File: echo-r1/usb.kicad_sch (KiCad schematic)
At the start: 14 parts, among them J2 TYPE-C-31-M-12, Q5 AO3401A, U8 USB3320C-EZK

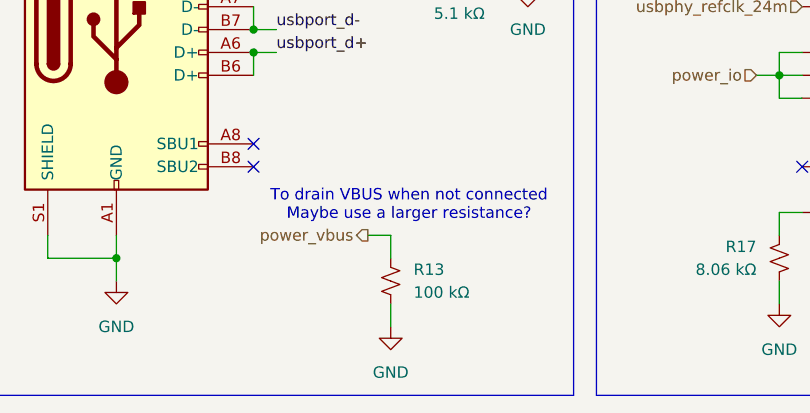
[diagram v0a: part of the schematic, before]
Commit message: R1-Rev1: remove VBUS discharge resistor
This is not needed since there is a path through the ADC
voltage divider to discharge VBUS -- and realistically
the battery charger should also discharge VBUS even with
no resistive path to ground.
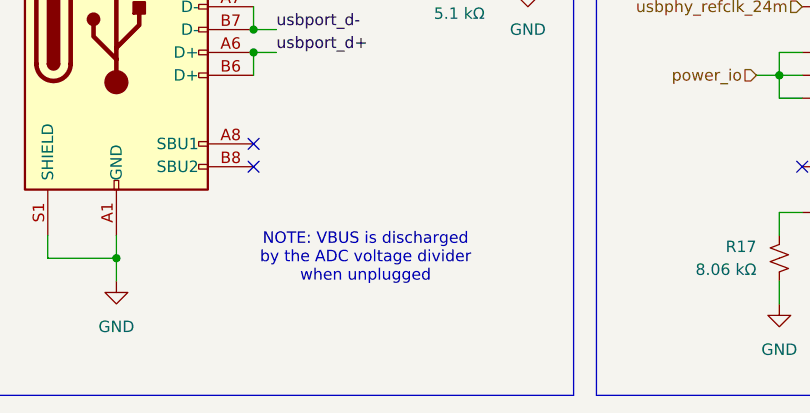
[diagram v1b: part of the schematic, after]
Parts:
- removed R13: 100 kΩ, Resistor_SMD:R_0402_1005Metric, symbol Device:R_Small_US
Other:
- note added: "NOTE: VBUS is discharged by the ADC voltage divider when unplugged"
- note removed: "To drain VBUS when not connected Maybe use a larger resistance?"
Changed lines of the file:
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@@
 		)
 	)
-	(text "To drain VBUS when not connected\nMaybe use a larger resistance?"
+	(text "NOTE: VBUS is discharged\nby the ADC voltage divider\nwhen unplugged"
 		(exclude_from_sim no)
-		(at 101.092 131.318 0)
+		(at 96.266 137.16 0)
 		(effects
 			(font
@@
 	(wire
 		(pts
-			(xy 99.06 142.24) (xy 99.06 144.78)
-		)
-		(stroke
-			(width 0)
-			(type default)
-		)
-	)
-	(wire
-		(pts
 			(xy 114.3 101.6) (xy 114.3 104.14)
 		)
@@
 	(wire
 		(pts
-			(xy 99.06 137.16) (xy 99.06 134.62)
-		)
-		(stroke
-			(width 0)
-			(type default)
-		)
-	)
-	(wire
-		(pts
 			(xy 236.22 66.04) (xy 236.22 63.5)
 		)
@@
 		)
 	)
-	(wire
-		(pts
-			(xy 99.06 134.62) (xy 96.52 134.62)
-		)
-		(stroke
-			(width 0)
-			(type default)
-		)
-	)
 	(label "ulpi.d2"
 		(at 185.42 104.14 0)
@@
 		)
 	)
-	(hierarchical_label "power_vbus"
-		(shape output)
-		(at 96.52 134.62 180)
-		(effects
-			(font
-				(size 1.27 1.27)
-			)
-			(justify right)
-		)
-	)
 	(hierarchical_label "power_io"
 		(shape input)
@@
 	(symbol
 		(lib_id "power:GND")
-		(at 99.06 144.78 0)
-		(unit 1)
-		(exclude_from_sim no)
-		(in_bom yes)
-		(on_board yes)
-		(dnp no)
-		(fields_autoplaced yes)
-		(property "Reference" "#PWR031"
-			(at 99.06 151.13 0)
-			(effects
-				(font
-					(size 1.27 1.27)
-				)
-				(hide yes)
-			)
-		)
-		(property "Value" "GND"
-			(at 99.06 149.86 0)
-			(effects
-				(font
-					(size 1.27 1.27)
-				)
-			)
-		)
-		(property "Footprint" ""
-			(at 99.06 144.78 0)
-			(effects
-				(font
-					(size 1.27 1.27)
-				)
-				(hide yes)
-			)
-		)
-		(property "Datasheet" ""
-			(at 99.06 144.78 0)
-			(effects
-				(font
-					(size 1.27 1.27)
-				)
-				(hide yes)
-			)
-		)
-		(property "Description" "Power symbol creates a global label with name \"GND\" , ground"
-			(at 99.06 144.78 0)
-			(effects
-				(font
-					(size 1.27 1.27)
-				)
-				(hide yes)
-			)
-		)
-		(pin "1"
-		)
-		(instances
-			(project ""
-				(path "/aa241847-30f4-429d-a148-6a6e39ba98e0/2bbed0e1-7a0b-4278-85a9-f432ea240e72"
-					(reference "#PWR031")
-					(unit 1)
-				)
-			)
-		)
-	)
-	(symbol
-		(lib_id "power:GND")
 		(at 142.24 142.24 0)
 		(unit 1)
@@
 					(unit 1)
 				)
-			)
-		)
-	)
-	(symbol
-		(lib_id "Device:R_Small_US")
-		(at 99.06 139.7 0)
-		(unit 1)
-		(exclude_from_sim no)
-		(in_bom yes)
-		(on_board yes)
-		(dnp no)
-		(fields_autoplaced yes)
-		(property "Reference" "R13"
-			(at 101.6 138.4299 0)
-			(effects
-				(font
-					(size 1.27 1.27)
-				)
-				(justify left)
-			)
-		)
-		(property "Value" "100 kΩ"
-			(at 101.6 140.9699 0)
-			(effects
-				(font
-					(size 1.27 1.27)
-				)
-				(justify left)
-			)
-		)
-		(property "Footprint" "Resistor_SMD:R_0402_1005Metric"
-			(at 99.06 139.7 0)
-			(effects
-				(font
-					(size 1.27 1.27)
-				)
-				(hide yes)
-			)
-		)
-		(property "Datasheet" "~"
-			(at 99.06 139.7 0)
-			(effects
-				(font
-					(size 1.27 1.27)
-				)
-				(hide yes)
-			)
-		)
-		(property "Description" "Resistor, small US symbol"
-			(at 99.06 139.7 0)
-			(effects
-				(font
-					(size 1.27 1.27)
-				)
-				(hide yes)
-			)
-		)
-		(property "LCSC#" "C60491"
-			(at 99.06 139.7 0)
-			(effects
-				(font
-					(size 1.27 1.27)
-				)
-				(hide yes)
-			)
-		)
-		(pin "1"
-		)
-		(pin "2"
-		)
-		(instances
-			(project ""
-				(path "/aa241847-30f4-429d-a148-6a6e39ba98e0/2bbed0e1-7a0b-4278-85a9-f432ea240e72"
-					(reference "R13")
-					(unit 1)
-				)

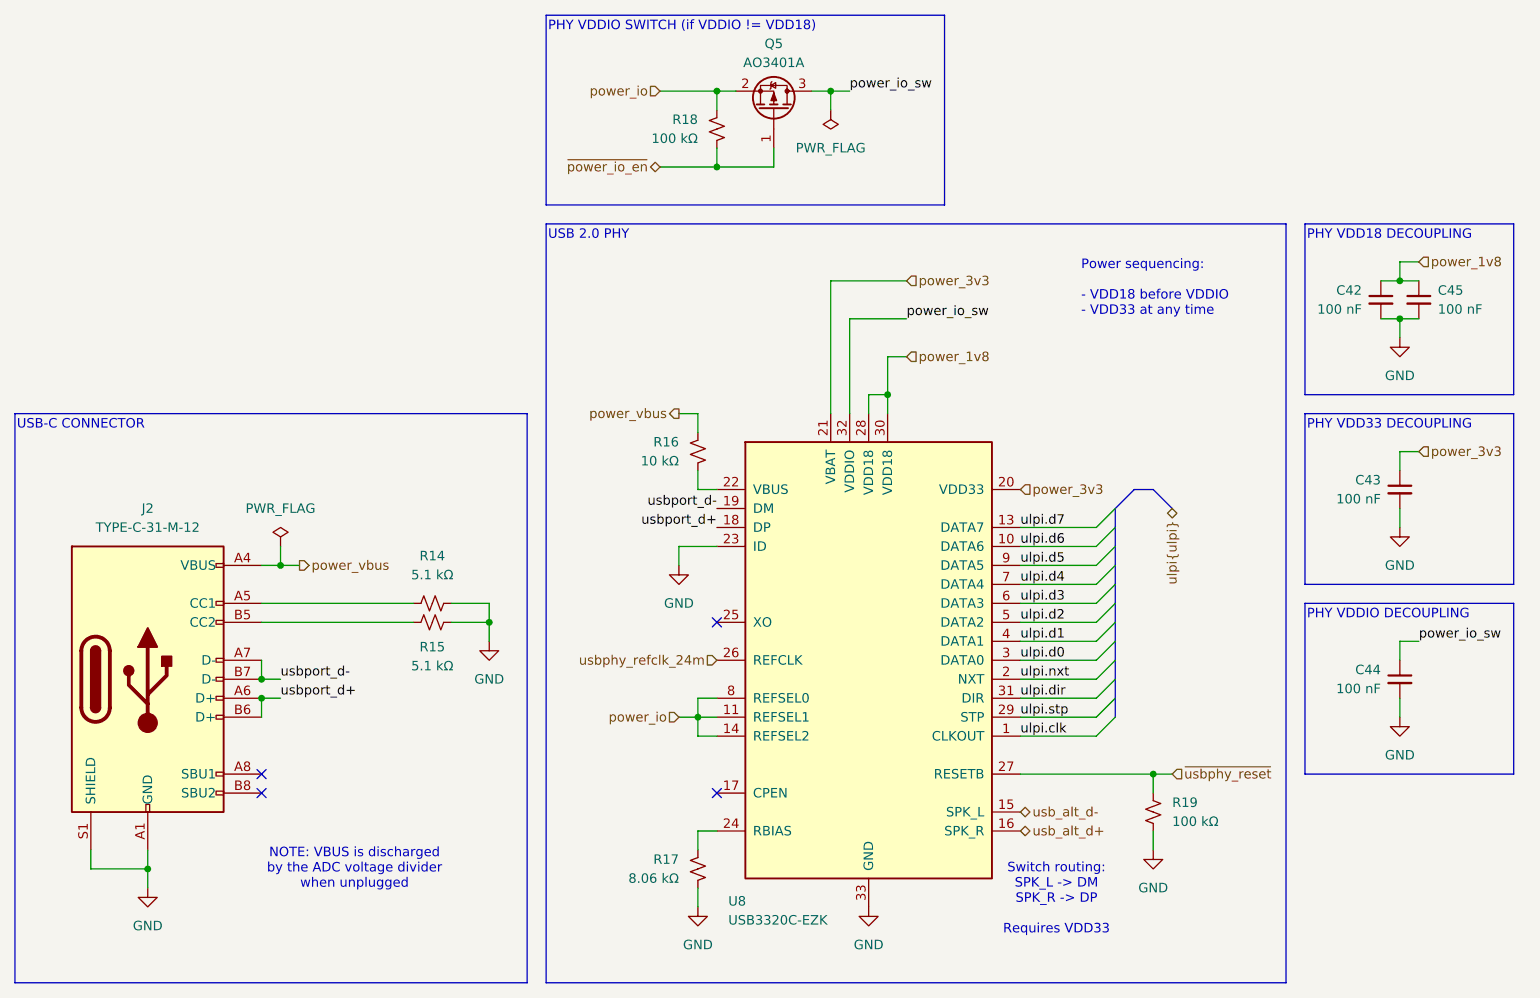
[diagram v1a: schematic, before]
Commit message: WIP redesign with STM32H7R3Z8J6
The H7R3 has a bunch of features that greatly simplify the design:
support for HyperRAM, which requires far fewer pins than SDRAM and
is more power efficient; this frees up the FMC to interface with the
display in 8-bit 8080 MCU mode; and there is a built-in USB HS PHY,
removing the need for an external PHY.

The huge reduction in signal count allows for a smaller pin count
package -- only 144 pins. HyperRAM only comes in BGA packages so it
makes sense to also use the UFBGA-144 package for the CPU, which
takes up less than 1/4 of the board area of an LQFP-176 package.
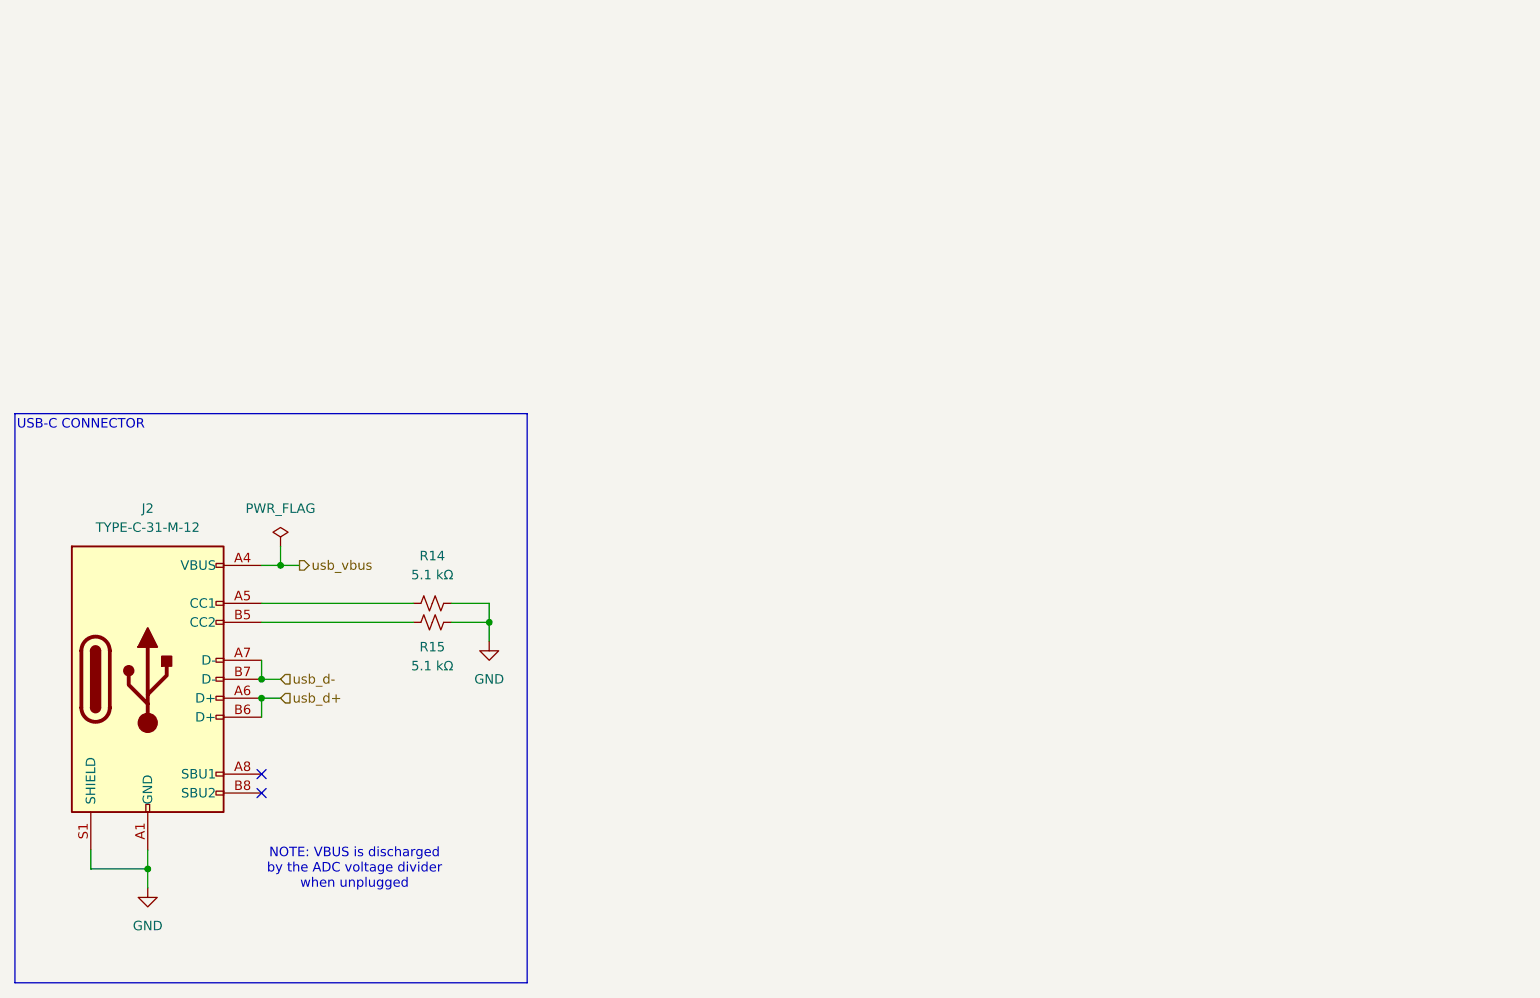
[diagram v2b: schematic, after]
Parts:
- removed C42, C43, C44, C45: 100 nF, Capacitor_SMD:C_0402_1005Metric, symbol Device:C_Small
- removed Q5: AO3401A, Package_TO_SOT_SMD:SOT-23, symbol Device:Q_PMOS_GSD
- removed R16: 10 kΩ, Resistor_SMD:R_0402_1005Metric, symbol Device:R_Small_US
- removed R17: 8.06 kΩ, Resistor_SMD:R_0402_1005Metric, symbol Device:R_Small_US
- removed R18, R19: 100 kΩ, Resistor_SMD:R_0402_1005Metric, symbol Device:R_Small_US
- removed U8: USB3320C-EZK, Package_DFN_QFN:QFN-32-1EP_5x5mm_P0.5mm_EP3.1x3.1mm_ThermalVias, symbol echoplayer:USB3320C-EZK
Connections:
- net power_vbus renamed usb_vbus
- net usbport_d+ renamed usb_d+
- net usbport_d- renamed usb_d-
- no-connect marks 4 -> 2
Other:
- note removed: "PHY VDD18 DECOUPLING"
- note removed: "PHY VDD33 DECOUPLING"
- note removed: "PHY VDDIO DECOUPLING"
- note removed: "PHY VDDIO SWITCH (if VDDIO != VDD18)"
- note removed: "Power sequencing: - VDD18 before VDDIO - VDD33 at any time"
- note removed: "Switch routing: SPK_L -> DM SPK_R -> DP Requires VDD33"
- note removed: "USB 2.0 PHY"
